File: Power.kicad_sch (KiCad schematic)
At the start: 35 parts, among them U3 STPMIC1APQR

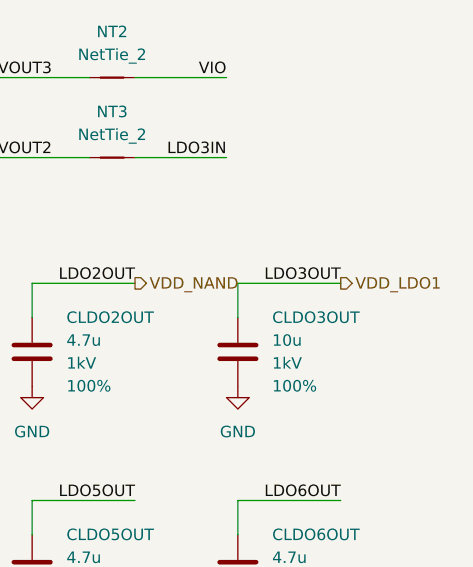
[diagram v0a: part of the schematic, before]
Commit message: Updated decoupling caps
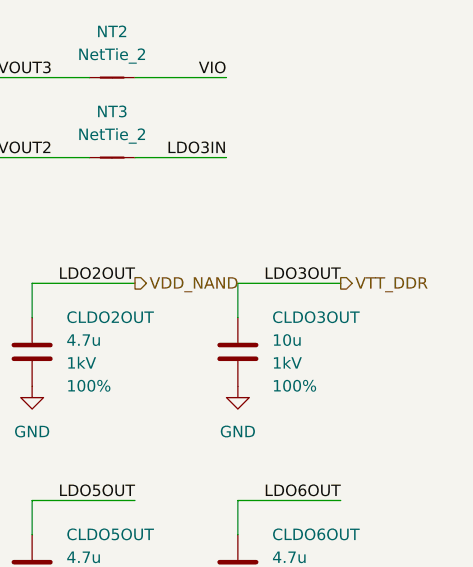
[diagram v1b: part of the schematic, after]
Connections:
- net VDD_LDO1 renamed VTT_DDR
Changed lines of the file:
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@@
 		)
 	)
-	(hierarchical_label "VDD_LDO1"
+	(hierarchical_label "VTT_DDR"
 		(shape output)
 		(at 271.78 116.84 0)

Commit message: Updating mandatory circuits
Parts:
- removed R1, R2: 2.2k, SparkFun-Resistor:R_0603_1608Metric, symbol SparkFun-Resistor:R
- added R22, R23: 2.2k, SparkFun-Resistor:R_0603_1608Metric, symbol SparkFun-Resistor:R
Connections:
- net SCL: now also R22.2
- net SDA: now also R23.2
- net VIO: now also R22.1, R23.1

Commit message: Added USB, power and other signals
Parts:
- R22, R23: value 2.2k -> 1.5k
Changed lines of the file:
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@@
 			)
 		)
-		(property "Value" "2.2k"
+		(property "Value" "1.5k"
 			(at 162.56 90.1699 90)
 			(effects
@@
 			)
 		)
-		(property "Value" "2.2k"
+		(property "Value" "1.5k"
 			(at 186.69 90.1699 90)
 			(effects

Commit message: Working on Ethernet connections
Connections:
- no-connect marks 0 -> 1
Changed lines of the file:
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@@
 		(color 0 0 0 0)
 	)
+	(no_connect
+		(at 63.5 78.74)
+	)
 	(wire
 		(pts
@@
 		)
 		(stroke
-			(width 0)
-			(type default)
-		)
-	)
-	(wire
-		(pts
-			(xy 50.8 78.74) (xy 63.5 78.74)
-		)
-		(stroke

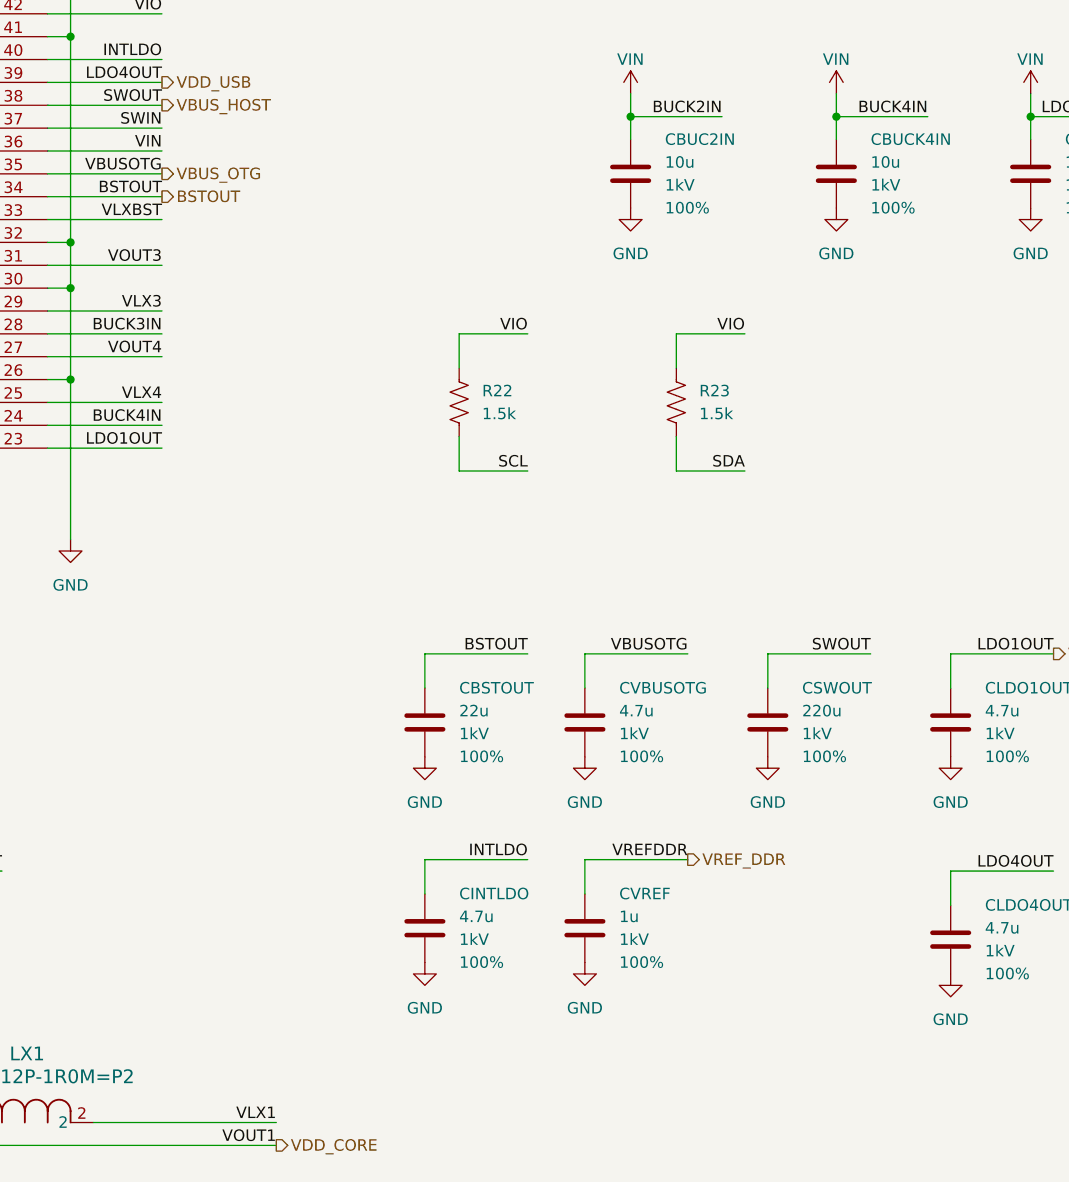
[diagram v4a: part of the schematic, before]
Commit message: Finished USB JTAG connectors and cleaned up schematic
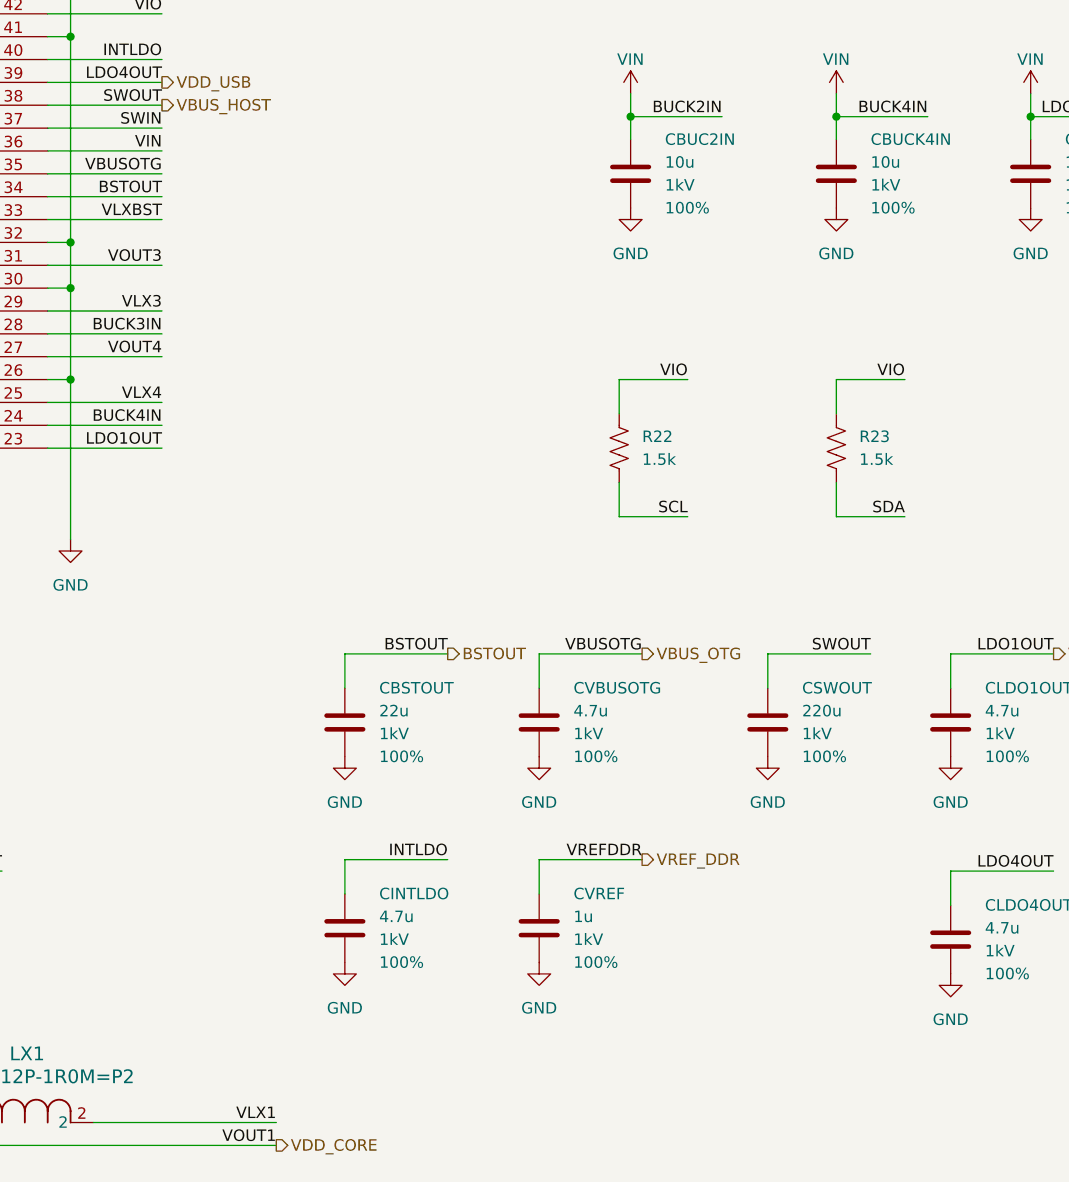
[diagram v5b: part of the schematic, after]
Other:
- moved on the sheet: CBSTOUT, CINTLDO, CVBUSOTG, CVREF, R22, R23

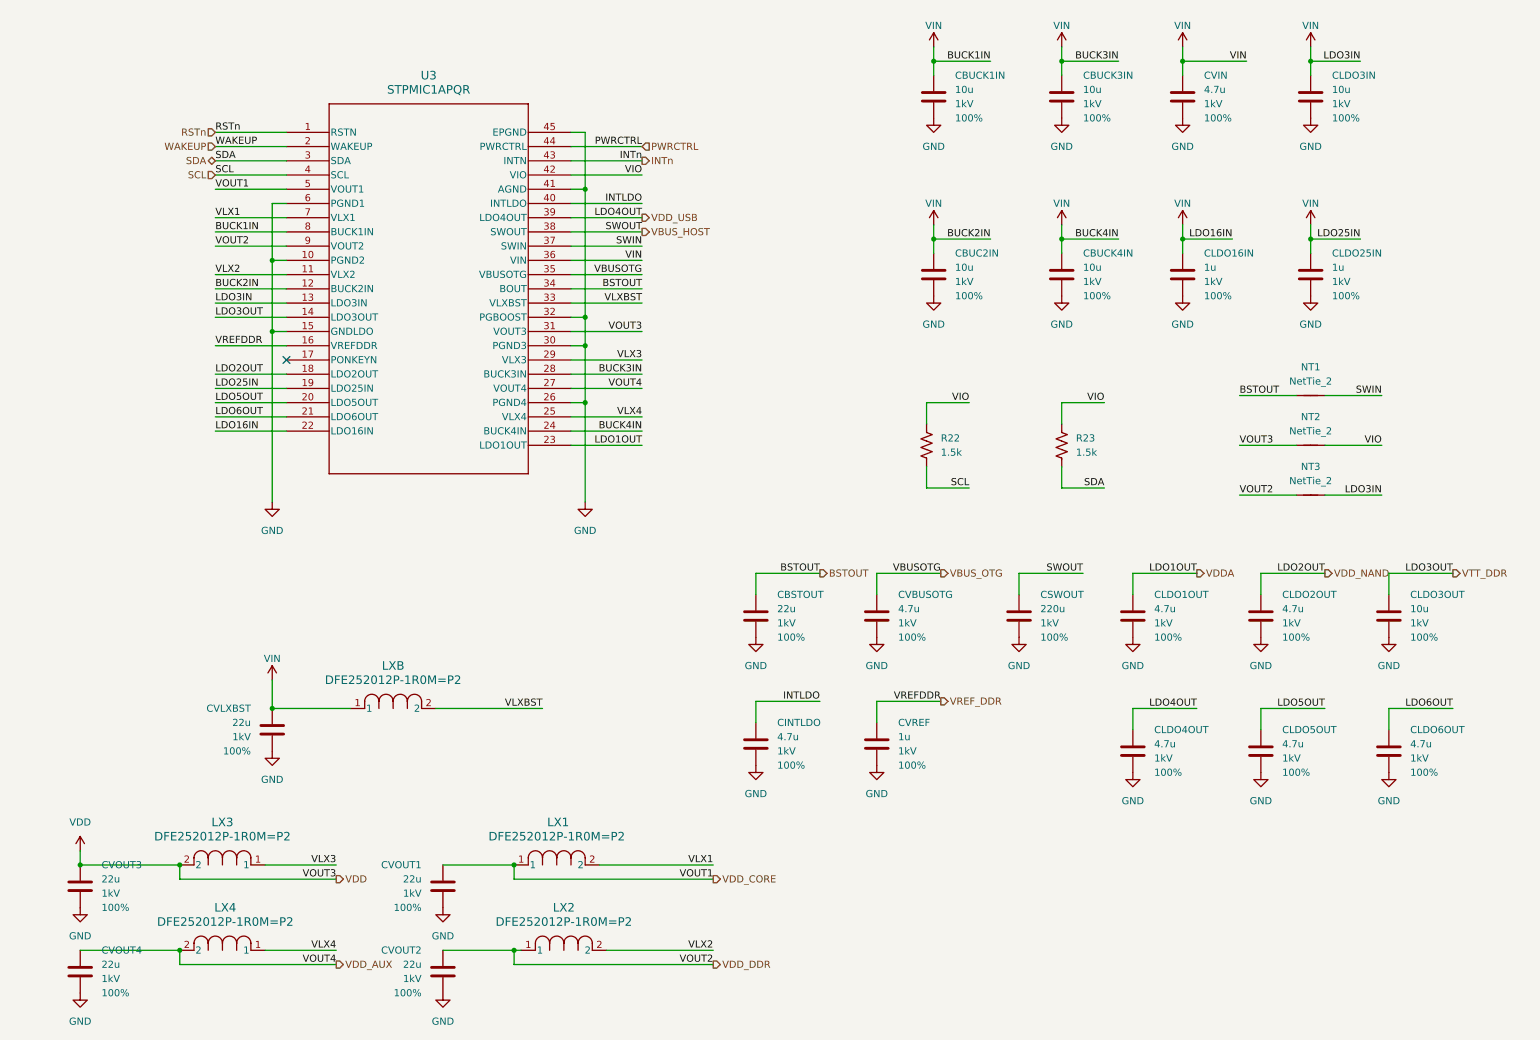
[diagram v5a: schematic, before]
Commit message: Adding more decoupling and started on DSI connector
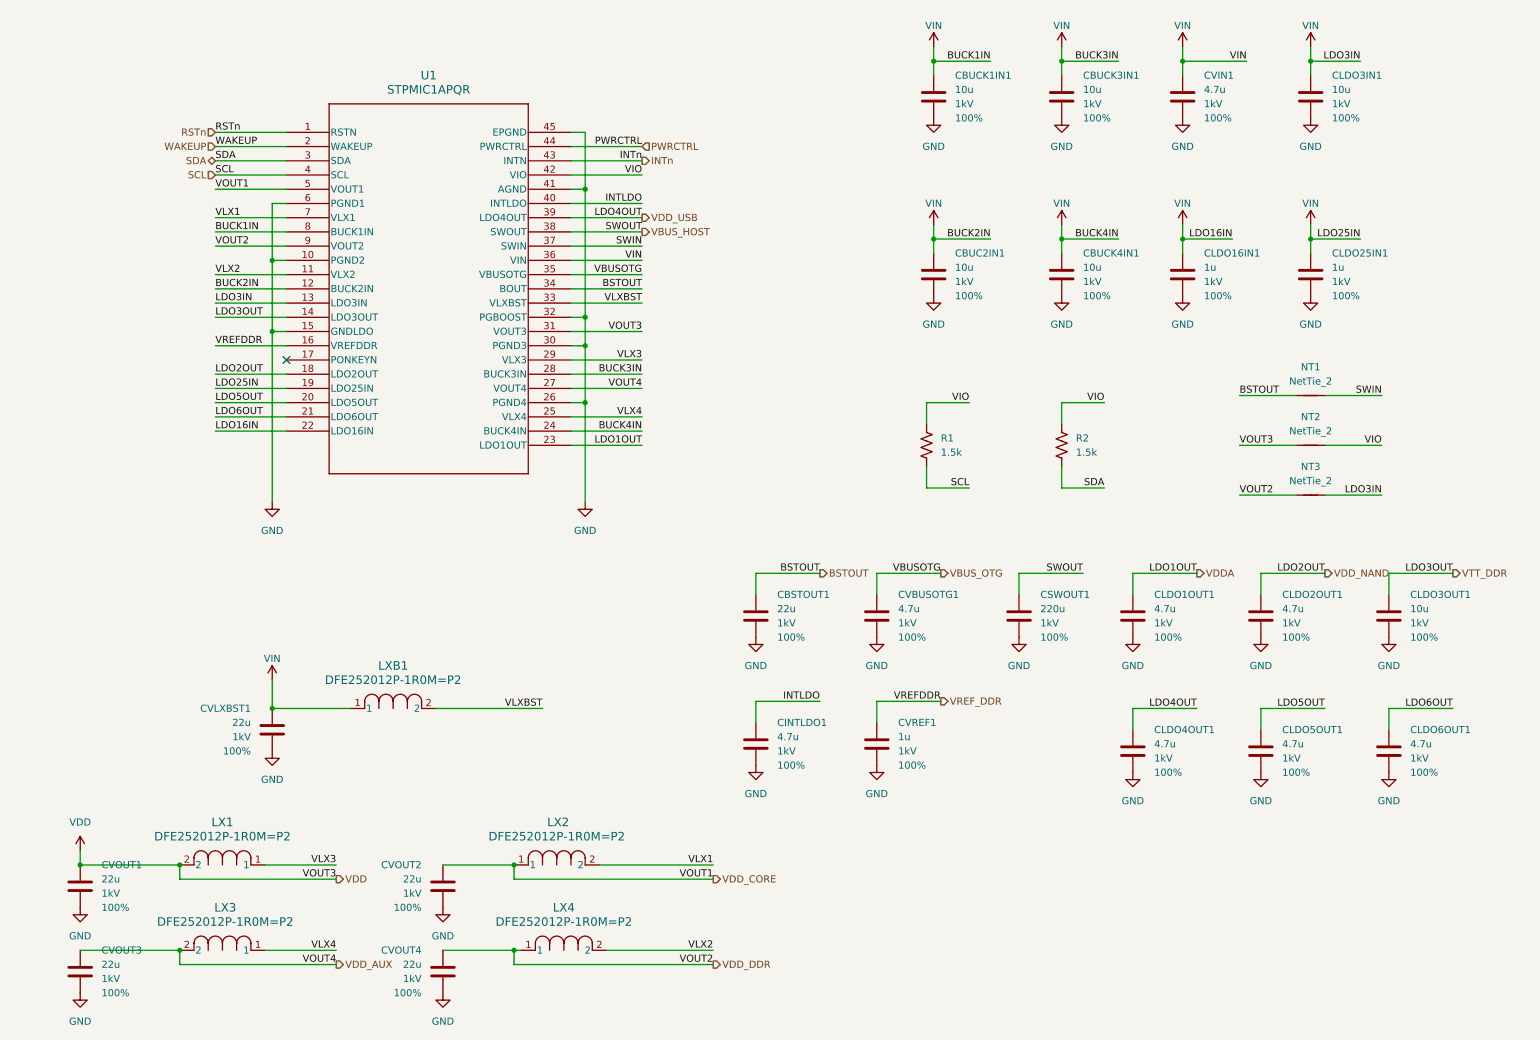
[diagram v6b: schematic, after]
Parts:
- CINTLDO1: renamed from CINTLDO; footprint 0402 -> (none)
- CLDO16IN1: renamed from CLDO16IN; footprint 0402 -> (none)
- CLDO1OUT1: renamed from CLDO1OUT; footprint 0402 -> (none)
- CLDO25IN1: renamed from CLDO25IN; footprint 0402 -> (none)
- CLDO2OUT1: renamed from CLDO2OUT; footprint 0402 -> (none)
- CLDO3IN1: renamed from CLDO3IN; footprint 0603 -> (none)
- CLDO3OUT1: renamed from CLDO3OUT; footprint 0603 -> (none)
- CLDO4OUT1: renamed from CLDO4OUT; footprint 0402 -> (none)
- CLDO5OUT1: renamed from CLDO5OUT; footprint 0402 -> (none)
- CLDO6OUT1: renamed from CLDO6OUT; footprint 0402 -> (none)
- CSWOUT1: renamed from CSWOUT; footprint 1206 -> (none)
- CVBUSOTG1: renamed from CVBUSOTG; footprint 0603 -> (none)
- CVIN1: renamed from CVIN; footprint 0402 -> (none)
- CVREF1: renamed from CVREF; footprint 0402 -> (none)
- LX1: renamed from LX3; footprint DFE252012P-1R0M=P2 -> (none)
- LX2: renamed from LX1; footprint DFE252012P-1R0M=P2 -> (none)
- LX3: renamed from LX4; footprint DFE252012P-1R0M=P2 -> (none)
- LX4: renamed from LX2; footprint DFE252012P-1R0M=P2 -> (none)
- LXB1: renamed from LXB; footprint DFE252012P-1R0M=P2 -> (none)
- U1: renamed from U3; footprint WFQFN44_5X6_STM -> (none)
- renumbered CBSTOUT to CBSTOUT1, CBUC2IN to CBUC2IN1, CBUCK1IN to CBUCK1IN1, CBUCK3IN to CBUCK3IN1, CBUCK4IN to CBUCK4IN1, CVLXBST to CVLXBST1, CVOUT3 to CVOUT1, CVOUT1 to CVOUT2, CVOUT4 to CVOUT3, CVOUT2 to CVOUT4, R22 to R1, R23 to R2

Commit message: Selecting footprints
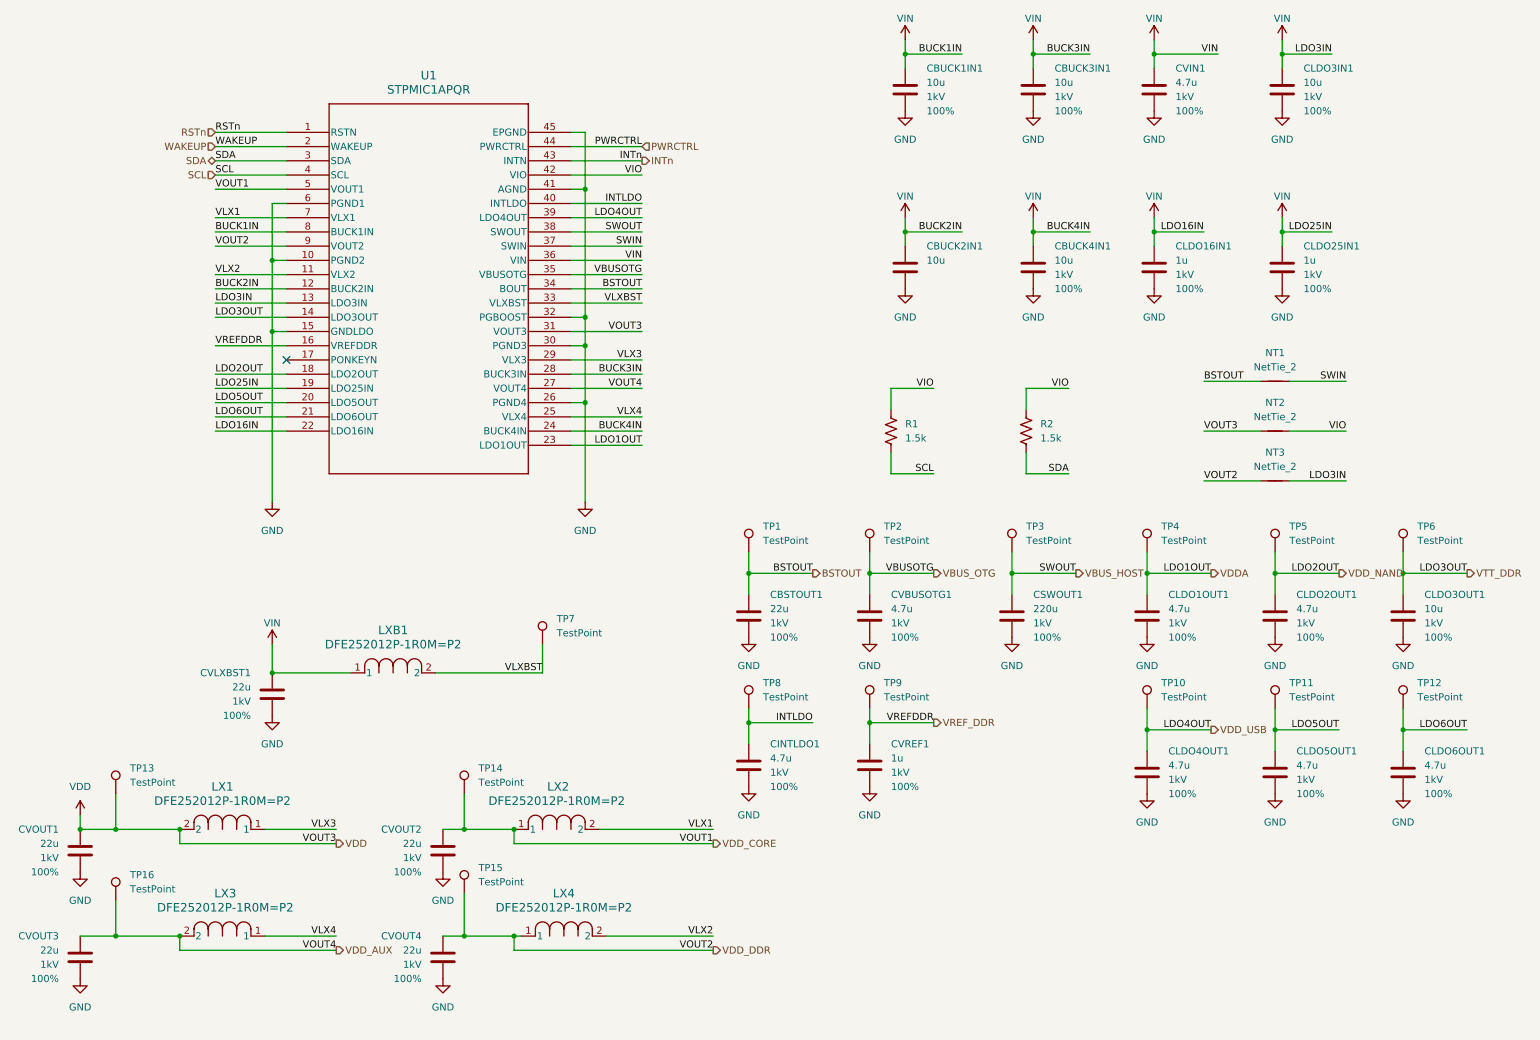
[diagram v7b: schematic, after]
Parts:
- added TP1, TP10, TP11, TP12, TP13, TP14, TP15, TP16, TP2, TP3, TP4, TP5, TP6, TP7, TP8, TP9: TestPoint, SparkFun-Connector:TestPoint-0.5mm, symbol Connector:TestPoint
- CBSTOUT1, CBUCK1IN1, CBUCK3IN1, CBUCK4IN1, CVLXBST1, CVOUT1, CVOUT2, CVOUT3, CVOUT4: footprint SparkFun-Capacitor:C_0603_1608Metric -> Capacitor_SMD:C_0603_1608Metric
- CBUCK2IN1: renamed from CBUC2IN1; footprint SparkFun-Capacitor:C_0603_1608Metric -> Capacitor_SMD:C_0603_1608Metric; Tolerance 100% -> (none); Voltage 1kV -> (none)
- CINTLDO1, CLDO16IN1, CLDO1OUT1, CLDO25IN1, CLDO2OUT1, CLDO4OUT1, CLDO5OUT1, CLDO6OUT1, CVIN1, CVREF1: footprint (none) -> Capacitor_SMD:C_0402_1005Metric
- CLDO3IN1, CLDO3OUT1, CVBUSOTG1: footprint (none) -> Capacitor_SMD:C_0603_1608Metric
- CSWOUT1: footprint (none) -> Capacitor_SMD:C_1206_3216Metric
- LX1, LX2, LX3, LX4, LXB1: footprint (none) -> Inductor_SMD:L_1008_2520Metric
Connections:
- net BSTOUT: now also TP1.1
- net INTLDO: now also TP8.1
- net LDO5OUT: now also TP11.1
- net LDO6OUT: now also TP12.1
- net VBUS_HOST: now also TP3.1
- net VBUS_OTG: now also TP2.1
- net VDD: now also TP13.1
- net VDDA: now also TP4.1
- net VDD_AUX: now also TP16.1
- net VDD_CORE: now also TP14.1
- net VDD_DDR: now also TP15.1
- net VDD_NAND: now also TP5.1
- net VDD_USB: now also TP10.1
- net VLXBST: now also TP7.1
- net VREF_DDR: now also TP9.1
- net VTT_DDR: now also TP6.1
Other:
- moved on the sheet: CBSTOUT1, CBUCK1IN1, CBUCK2IN1, CBUCK3IN1, CBUCK4IN1, CINTLDO1, CLDO16IN1, CLDO1OUT1, CLDO25IN1, CLDO2OUT1, CLDO3IN1, CLDO3OUT1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

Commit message: Added all footprints and kicked off pcb design
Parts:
- NT1, NT2, NT3: footprint (none) -> NetTie:NetTie-2_SMD_Pad0.5mm
- U1: footprint (none) -> footprints:WFQFN44_5X6_STM
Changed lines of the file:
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@@
 			)
 		)
-		(property "Footprint" ""
+		(property "Footprint" "NetTie:NetTie-2_SMD_Pad0.5mm"
 			(at 240.03 82.55 0)
 			(effects
@@
 			)
 		)
-		(property "Footprint" ""
+		(property "Footprint" "NetTie:NetTie-2_SMD_Pad0.5mm"
 			(at 240.03 91.44 0)
 			(effects
@@
 			)
 		)
-		(property "Footprint" ""
+		(property "Footprint" "footprints:WFQFN44_5X6_STM"
 			(at 63.5 38.1 0)
 			(effects
@@
 			)
 		)
-		(property "Footprint" ""
+		(property "Footprint" "NetTie:NetTie-2_SMD_Pad0.5mm"
 			(at 240.03 100.33 0)
 			(effects
